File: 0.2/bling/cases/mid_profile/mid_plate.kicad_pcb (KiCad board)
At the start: 2 copper layers, 110.3 x 98 mm, 0 parts

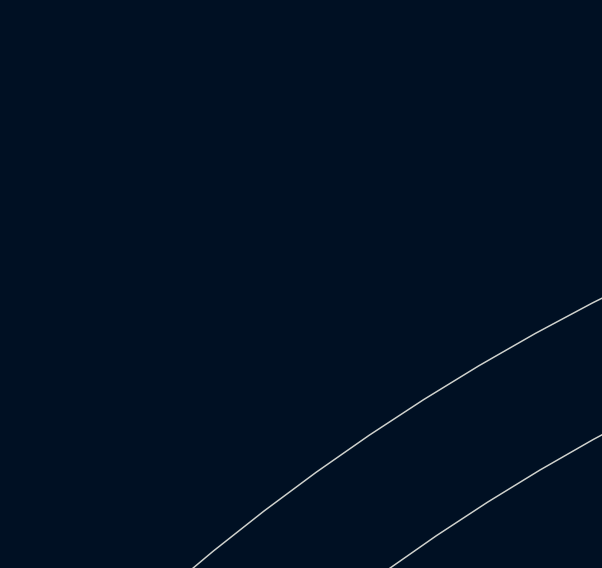
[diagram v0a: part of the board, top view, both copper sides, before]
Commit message: Add dummy component to each plate case
This works around a segfault in Pcbdraw which prevents renders in the
edge case where a PCB file has no module.
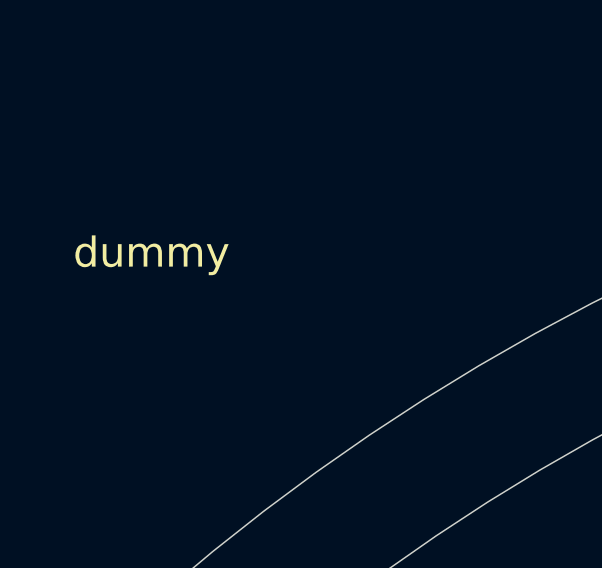
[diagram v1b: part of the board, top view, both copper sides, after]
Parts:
- added dummy: dummy, dummy:dummy, F.Cu at (12.0, 12.0)
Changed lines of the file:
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@@
     (tracks 0)
     (zones 0)
-    (modules 0)
+    (modules 1)
     (nets 1)
   )
@@
     (uvia_drill 0.1)
   )
+  (module dummy:dummy (layer F.Cu)
+    (at 12 12)
+    (fp_text reference dummy (at 0 0.5) (layer F.SilkS)
+      (effects (font (size 1 1) (thickness 0.15)))
+    )
+    (fp_text value dummy (at 0 -0.5) (layer F.Fab)
+      (effects (font (size 1 1) (thickness 0.15)))
+    )
+  )
   (gr_arc (start 15.089318 406.95507) (end 82.995848 94.415389) (angle -12.12538542) (layer Edge.Cuts) (width 0.05))
